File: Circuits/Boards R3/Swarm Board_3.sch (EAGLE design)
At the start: 149 parts, among them CON1 ISP(2X3), CON2 MAIN_CONNECTOR_14, CON5 HEADER_3X1, CON7 MAIN_CONNECTOR_8, M1 VIBMOTOR, SW1 CL-SB-22A, T1 TEFT4300, T10 TEFT4300, T11 NPN2N2222, T12 SI2333DS-T1, T13 NPN2N2222, T14 NPN2N2222, T15 NPN2N2222, T16 NPN2N2222, T17 NPN2N2222, T18 NPN2N2222, T19 IRLML6244TR, T2 TEFT4300, T20 IRLML6244TR, T21 IRLML6244TR, T22 IRLML6244TR, T23 IRLML6244TR, T3 NPN2N2222, T4 TEFT4300, T5 TEFT4300, T6 TEFT4300, T7 TEFT4300, T8 TEFT4300, T9 TEFT4300, U2 MCP73833, U3 ATMEGA1281, U4 MCP9700A, U5 AH182, U6 AH182, U7 QRE1113, U8 QRE1113

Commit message: Created BOMS
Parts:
- LED1: value red -> RED
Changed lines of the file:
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@@
 <part name="P+19" library="Supply" deviceset="+VRAW" device=""/>
 <part name="P+2" library="Supply" deviceset="+VRAW" device=""/>
-<part name="LED1" library="Passive" deviceset="LED" device="0603" value="red"/>
+<part name="LED1" library="Passive" deviceset="LED" device="0603" value="RED"/>
 <part name="R1" library="Passive" deviceset="RES" device="0603" value="1.5k"/>
 <part name="R2" library="Passive" deviceset="RES" device="0603" value="1k"/>

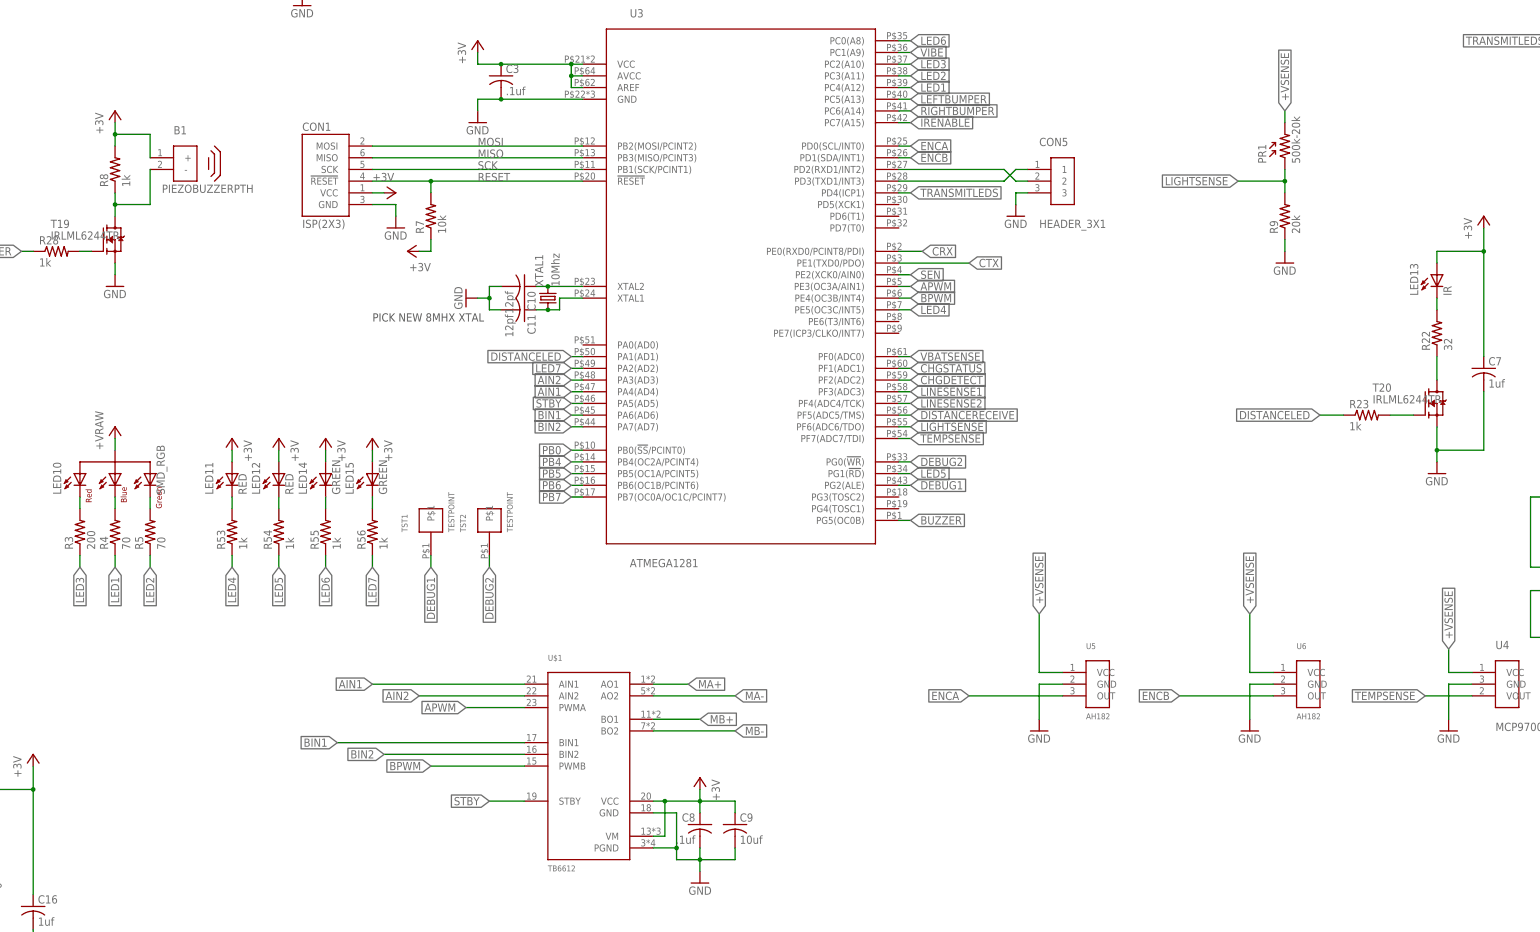
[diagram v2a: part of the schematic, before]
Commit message: BOMS and boards updated with a few slight value changes to reflect component availability
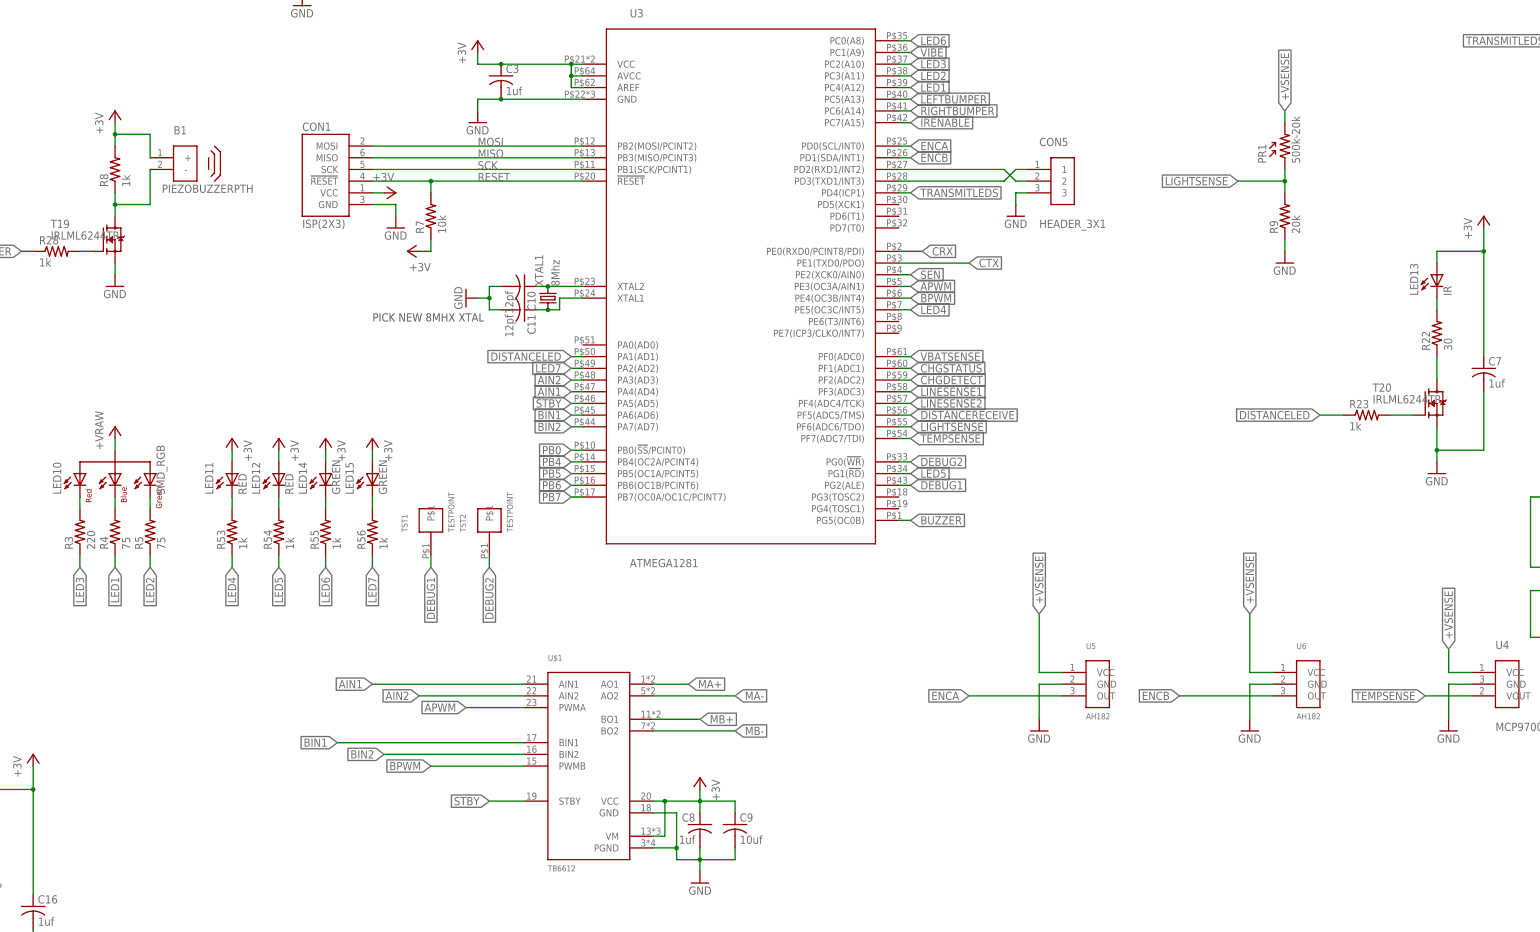
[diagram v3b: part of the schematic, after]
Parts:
- C3, C8: value .1uf -> 1uf
- R22: value 32 -> 30
- R3: value 200 -> 220
- R4, R5: value 70 -> 75
- XTAL1: value 10Mhz -> 8Mhz
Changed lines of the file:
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@@
 <part name="C1" library="Passive" deviceset="CAP" device="0603" value="1uf"/>
 <part name="GND2" library="Supply" deviceset="GND" device=""/>
-<part name="C3" library="Passive" deviceset="CAP" device="0603" value=".1uf"/>
+<part name="C3" library="Passive" deviceset="CAP" device="0603" value="1uf"/>
 <part name="R7" library="Passive" deviceset="RES" device="0603" value="10k"/>
 <part name="P+6" library="Supply" deviceset="+3V" device=""/>
@@
 <part name="C6" library="Passive" deviceset="CAP" device="0805" value="10uf"/>
 <part name="P+9" library="Supply" deviceset="+3V" device=""/>
-<part name="R22" library="Passive" deviceset="RES" device="0603" value="32"/>
+<part name="R22" library="Passive" deviceset="RES" device="0603" value="30"/>
 <part name="R23" library="Passive" deviceset="RES" device="0603" value="1k"/>
 <part name="GND9" library="Supply" deviceset="GND" device=""/>
@@
 <part name="GND14" library="Supply" deviceset="GND" device=""/>
 <part name="GND15" library="Supply" deviceset="GND" device=""/>
-<part name="C8" library="Passive" deviceset="CAP" device="0603" value=".1uf"/>
+<part name="C8" library="Passive" deviceset="CAP" device="0603" value="1uf"/>
 <part name="GND16" library="Supply" deviceset="GND" device=""/>
 <part name="P+12" library="Supply" deviceset="+3V" device=""/>
@@
 <part name="R33" library="Passive" deviceset="RES" device="0603" value="22k"/>
 <part name="R35" library="Passive" deviceset="RES" device="0603" value="22k"/>
-<part name="XTAL1" library="Passive" deviceset="NX5032GA-10.000000MHZ" device="" value="10Mhz"/>
+<part name="XTAL1" library="Passive" deviceset="NX5032GA-10.000000MHZ" device="" value="8Mhz"/>
 <part name="C10" library="Passive" deviceset="CAP" device="0603" value="12pf"/>
 <part name="C11" library="Passive" deviceset="CAP" device="0603" value="12pf"/>
@@
 <part name="LED10" library="Passive" deviceset="SMD_RGB" device=""/>
 <part name="P+20" library="Supply" deviceset="+VRAW" device=""/>
-<part name="R3" library="Passive" deviceset="RES" device="0603" value="200"/>
-<part name="R4" library="Passive" deviceset="RES" device="0603" value="70"/>
-<part name="R5" library="Passive" deviceset="RES" device="0603" value="70"/>
+<part name="R3" library="Passive" deviceset="RES" device="0603" value="220"/>
+<part name="R4" library="Passive" deviceset="RES" device="0603" value="75"/>
+<part name="R5" library="Passive" deviceset="RES" device="0603" value="75"/>
 <part name="CON5" library="Mechanical" deviceset="HEADER_3X1" device=""/>
 <part name="U3" library="DigitalIC" deviceset="ATMEGA1281" device=""/>
